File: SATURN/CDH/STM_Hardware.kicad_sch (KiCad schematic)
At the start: 15 parts, among them J3 SWD Pins, J4 USB_OTG, U3 RV-3028-C7 32.768KHZ 1PPM-TA-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, U4 TS3USB221ARSER, U5 USBLC6-4SC6

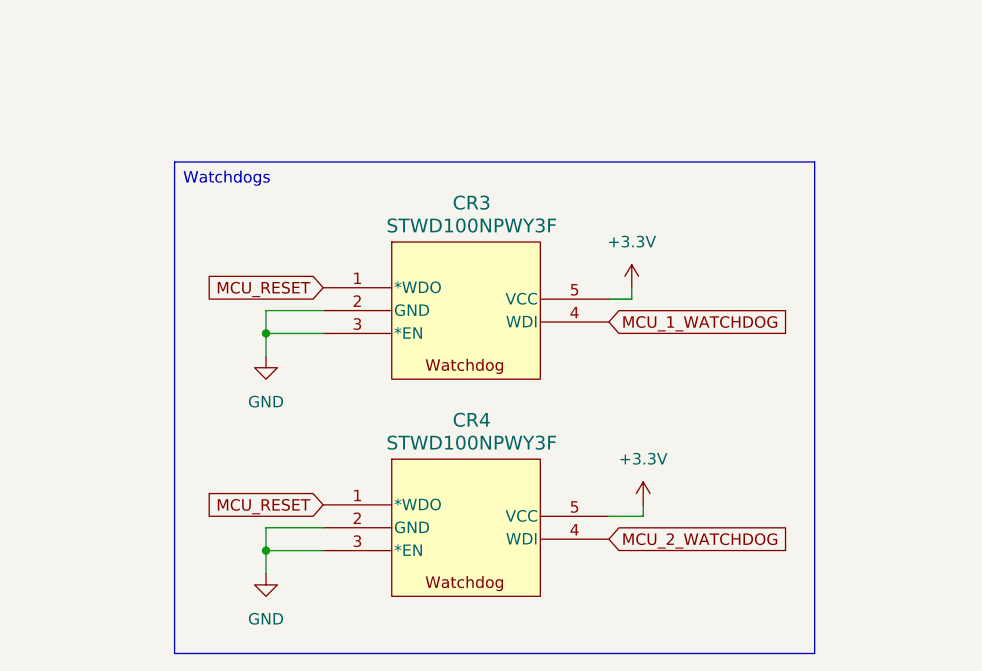
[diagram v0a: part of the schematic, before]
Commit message: Added memory, connections to MCUs
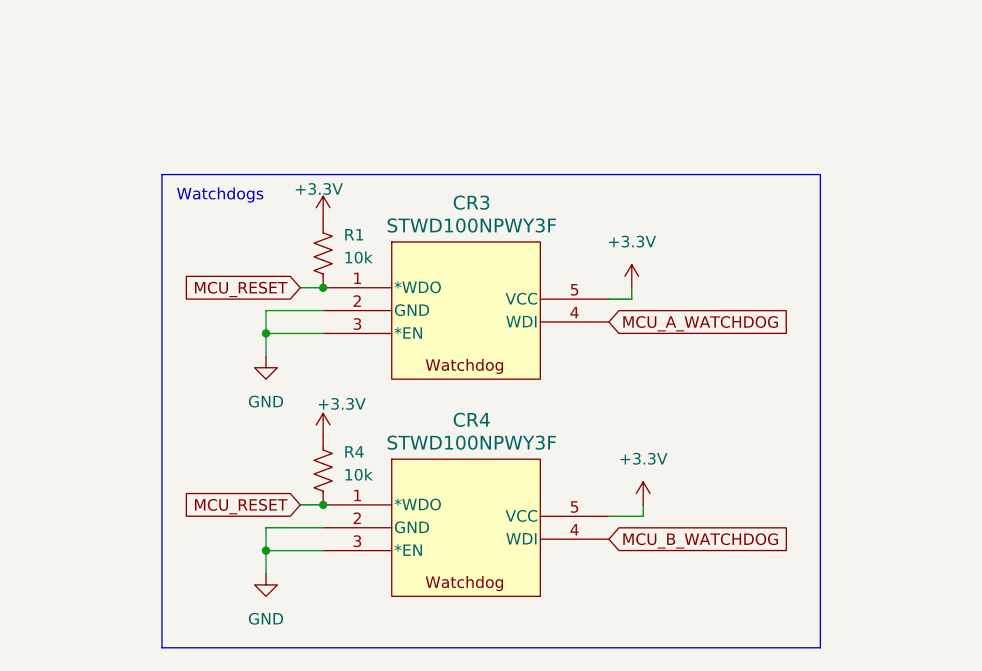
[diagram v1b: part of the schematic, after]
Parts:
- added R1, R4: 10k, symbol Device:R_US
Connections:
- net +3.3V: now also R1.1, R4.1
- net MCU_RESET: now also R1.2, R4.2
- net MCU_1_WATCHDOG renamed MCU_A_WATCHDOG
- net MCU_2_WATCHDOG renamed MCU_B_WATCHDOG
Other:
- note added: "Watchdogs"
